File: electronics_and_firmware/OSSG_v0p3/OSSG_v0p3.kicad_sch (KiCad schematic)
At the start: 65 parts, among them IC1 DW01A, J1 USB_B_Micro, Q1 FS8205A, Q2 Q_NPN_BEC, Q3 Q_NPN_BEC, SW1 SW_SPST, U1 ESP32-PICO-D4, U2 TP4056, U3 XC6222B331MRG, U4 FT232RQ, U5 APX803L-29SA-7

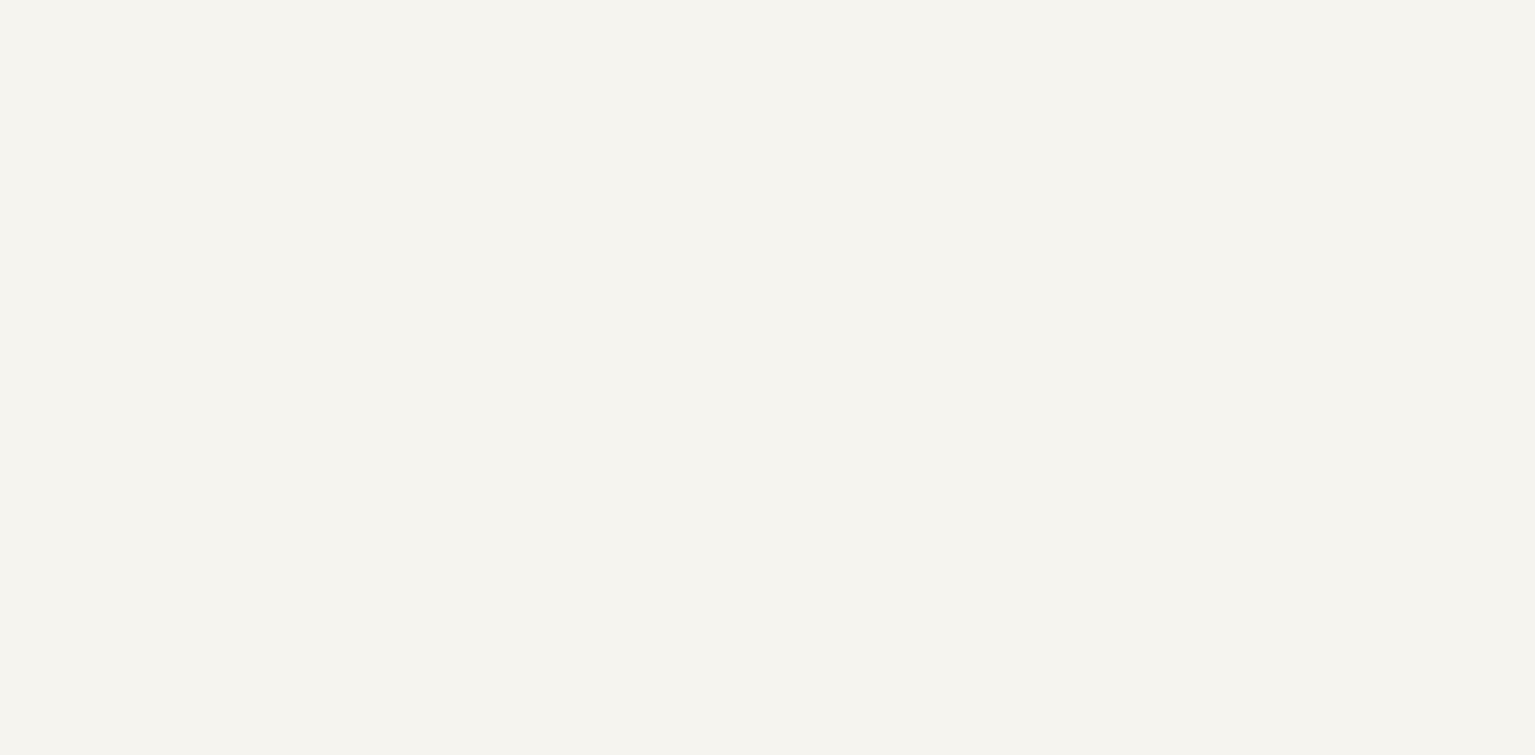
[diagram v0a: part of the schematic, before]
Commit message: add microphone and external microphone breakout pads to left arm board schematic and layout
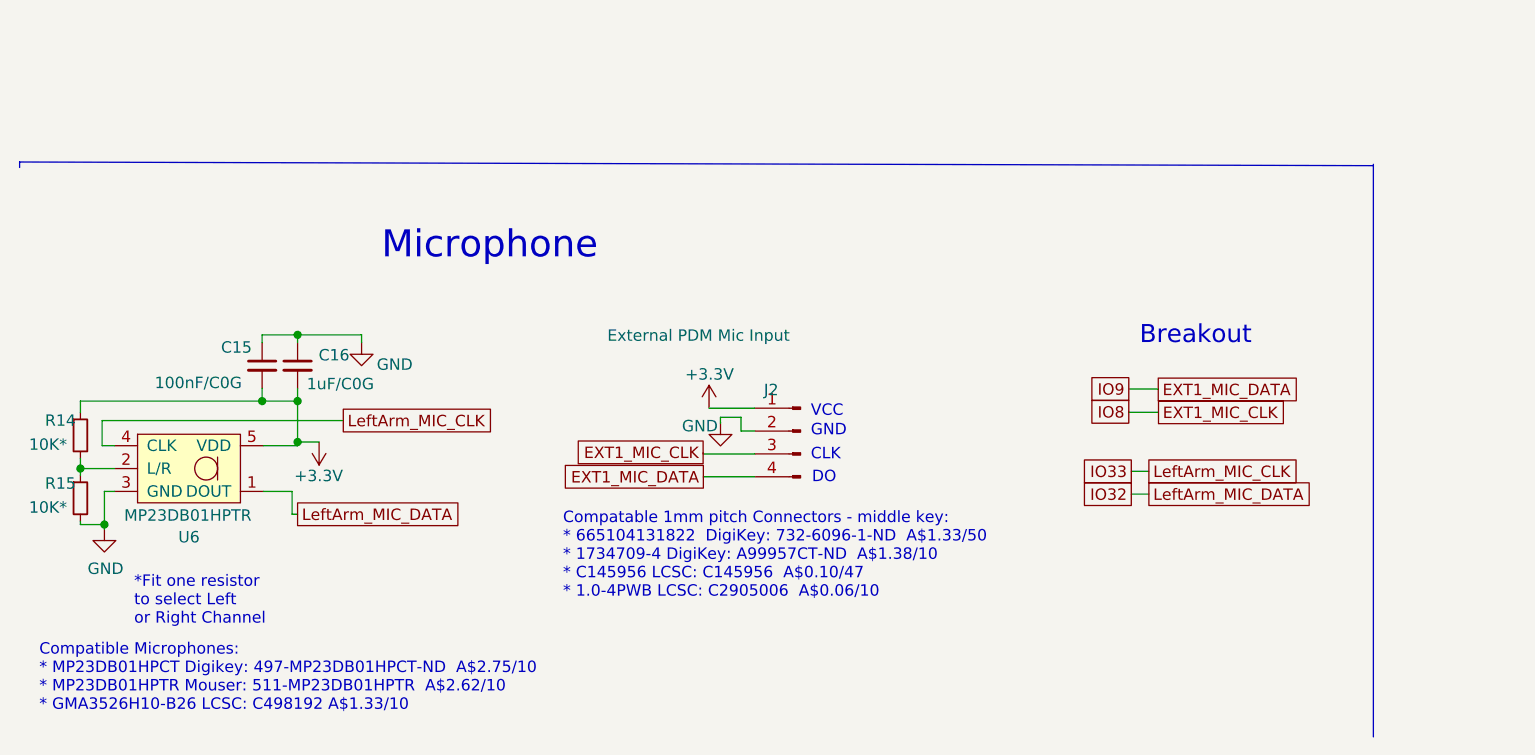
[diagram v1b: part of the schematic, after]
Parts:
- added C15: 100nF/C0G, Capacitor_SMD:C_0402_1005Metric, symbol Device:C_Small
- added C16: 1uF/C0G, Capacitor_SMD:C_0402_1005Metric, symbol Device:C_Small
- added J2: External PDM Mic Input, footprints:Solder-4P-Connector, symbol Connector:Conn_01x04_Male
- added R14, R15: 10K*, Resistor_SMD:R_0402_1005Metric, symbol Device:R_Small
- added U6: MP23DB01HPTR, footprints:MP23DB01HPTR, symbol microphone-rescue:MP23DB01HPTR-Pauls_Symbol_Library
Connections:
- net +3V3: now also C15.2, C16.2, J2.1 (Pin_1), R14.1, U6.5 (VDD)
- net GND: now also C15.1, C16.1, J2.2 (Pin_2), R15.2, U6.3 (GND)
- net IO32: now also U6.1 (DOUT)
- net IO33: now also U6.4 (CLK)
- net IO8 renamed EXT1_MIC_CLK
- net EXT1_MIC_CLK: now also J2.3 (Pin_3)
- net IO9 renamed EXT1_MIC_DATA
- net EXT1_MIC_DATA: now also J2.4 (Pin_4)
- new net: R14.2, R15.1, U6.2 (L/R)
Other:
- note added: "*Fit one resistor to select Left or Right Channel"
- note added: "CLK"
- note added: "Compatable 1mm pitch Connectors - middle key: * 665104131822 DigiKey: 732-6096-1-ND A$1.33/50 * 1734709-4 DigiKey: A99957CT-ND A$1.38/10 * C145956 LCSC: C145956 A$0.10/47 * 1.0-4PWB LCSC: C2905006 A$0.06/10"
- note added: "Compatible Microphones: * MP23DB01HPCT Digikey: 497-MP23DB01HPCT-ND A$2.75/10 * MP23DB01HPTR Mouser: 511-MP23DB01HPTR A$2.62/10 * GMA3526H10-B26 LCSC: C498192 A$1.33/10"
- note added: "DO"
- note added: "GND"
- note added: "Microphone"
- note added: "VCC"

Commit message: Layout and schematic tidying
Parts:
- C10, C11, C13: value C_Small -> NC
- C14: value C_Small -> Fine Tuning
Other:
- moved on the sheet: C1, C3, C4, C6, C7, Q2, Q3, R2, R6, R7, SW1

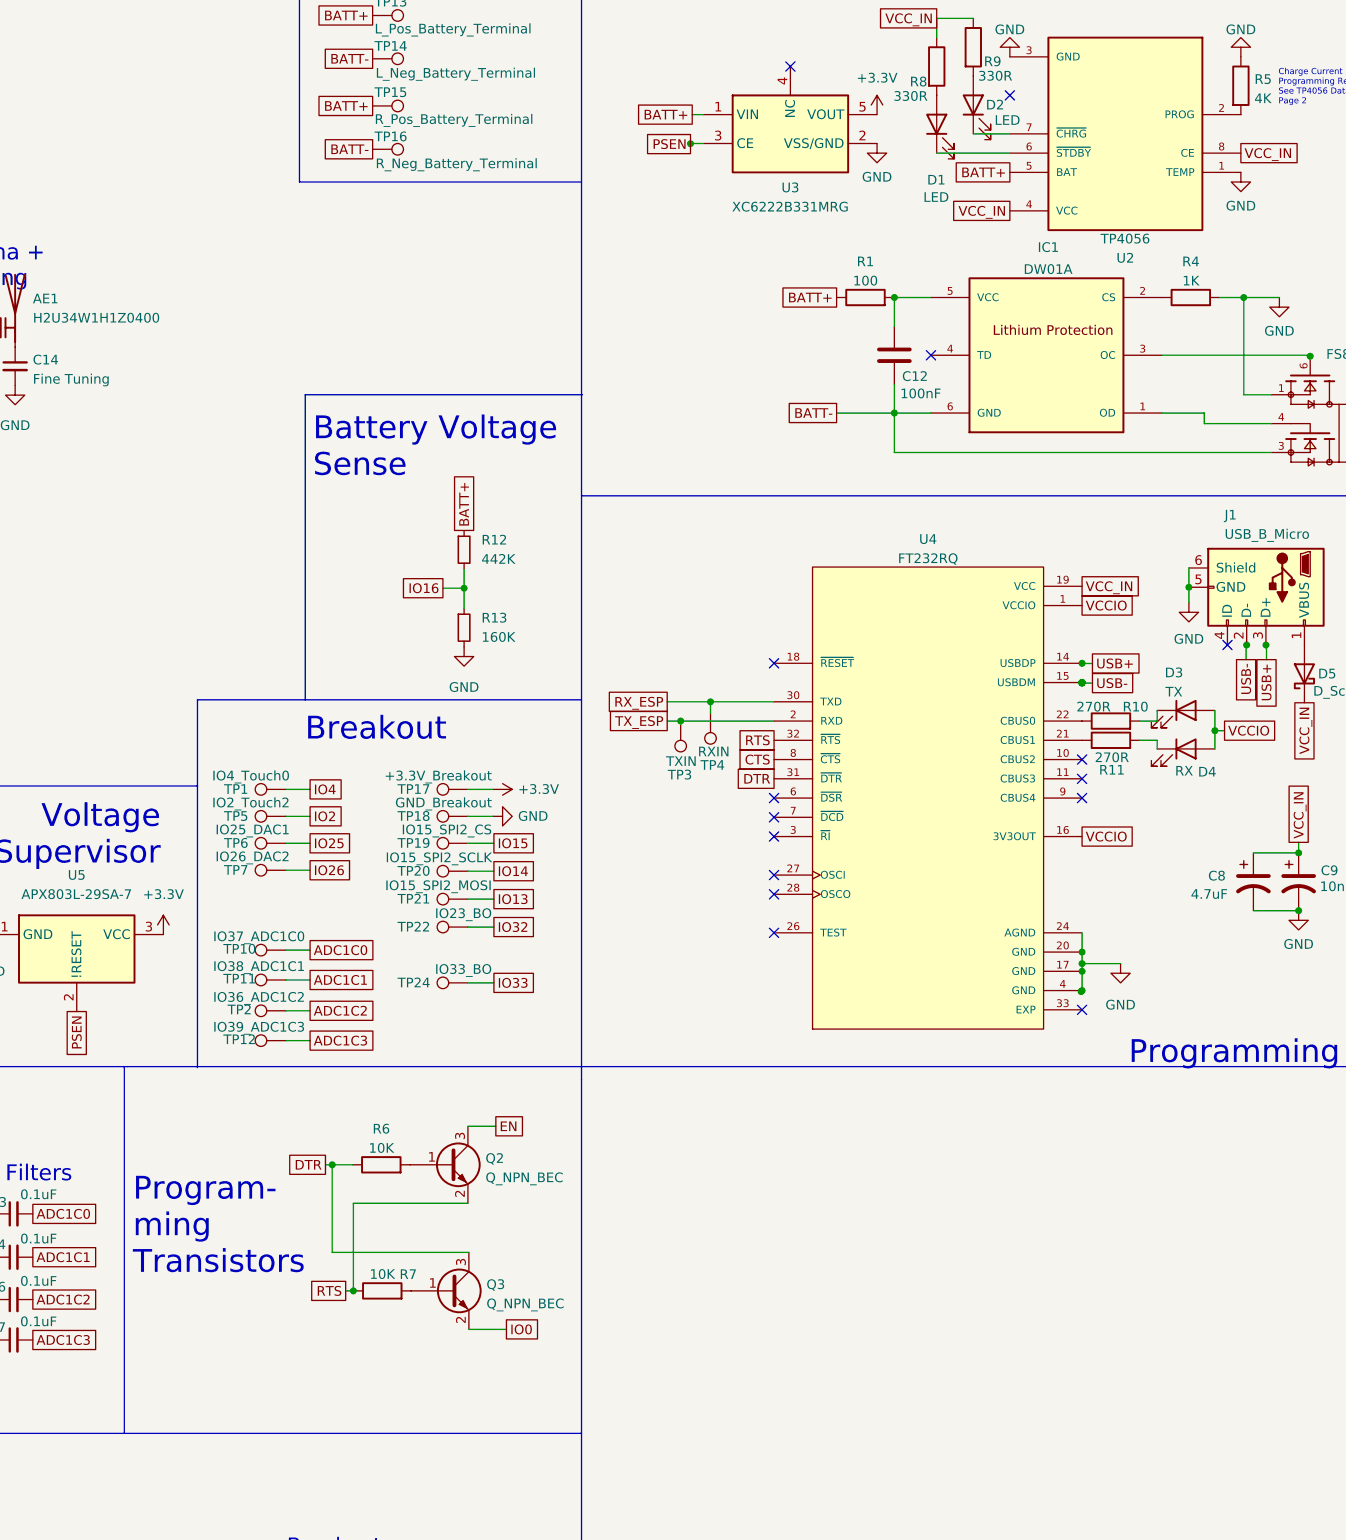
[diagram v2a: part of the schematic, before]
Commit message: add io0 and en TPs, fix silk screen, add missing capacitors, add ground pour and exposed pad for thermals under ESP32-PICO-D4
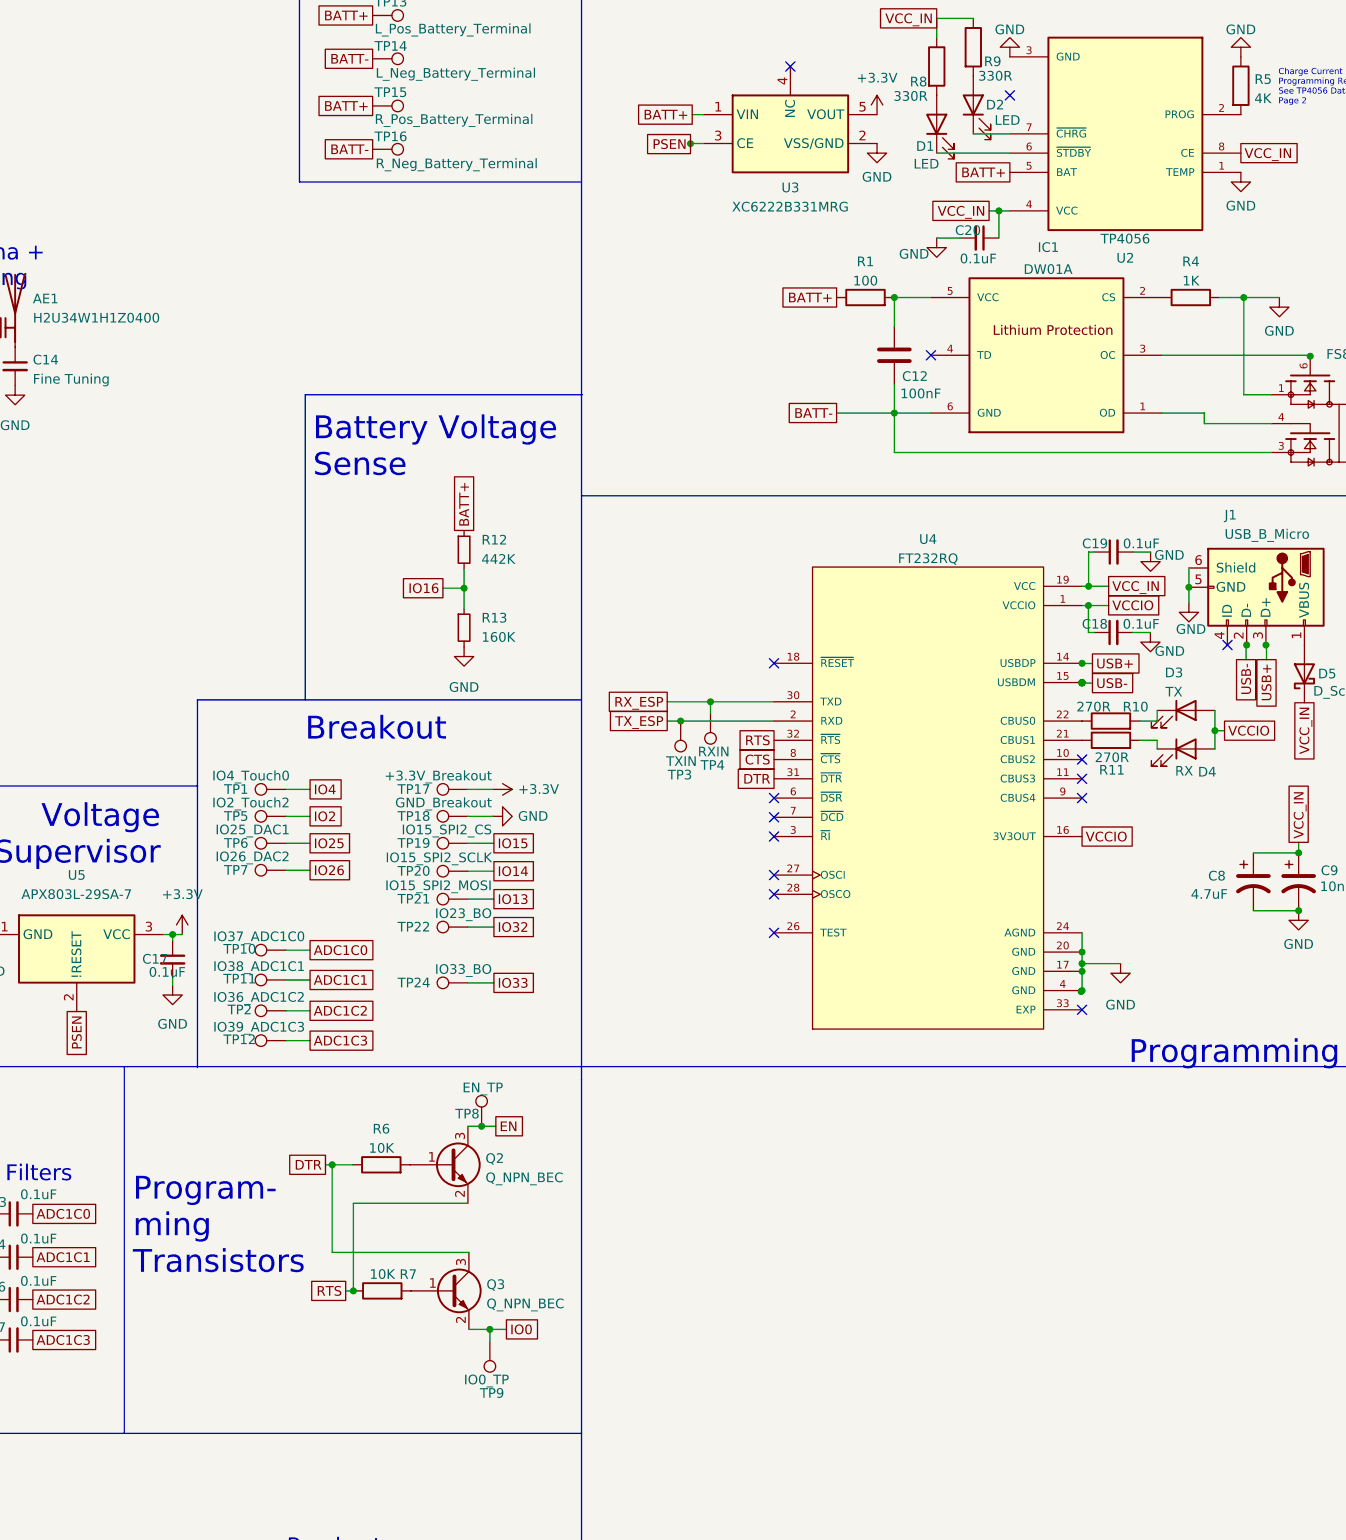
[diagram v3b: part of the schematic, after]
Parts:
- added C17, C18, C19, C20: 0.1uF, Capacitor_SMD:C_0402_1005Metric, symbol Device:C_Small
- added TP8: EN_TP, TestPoint:TestPoint_Pad_D1.0mm, symbol Connector:TestPoint
- added TP9: IO0_TP, TestPoint:TestPoint_Pad_D1.0mm, symbol Connector:TestPoint
- U3: DigiKeyLink (none) -> https://www.digikey.ca/en/products/detail/torex-semiconduct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; MPN (none) -> 893-1143-1-ND
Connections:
- net +3V3: now also C17.1
- net EN: now also TP8.1
- net GND: now also C17.2, C18.2, C19.2, C20.2
- net IO0: now also TP9.1
- net VCCIO: now also C18.1
- net VCC_IN: now also C19.1, C20.1
